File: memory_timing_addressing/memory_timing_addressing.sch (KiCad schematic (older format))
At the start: 1 part, among them P1 DIN_41612_128P

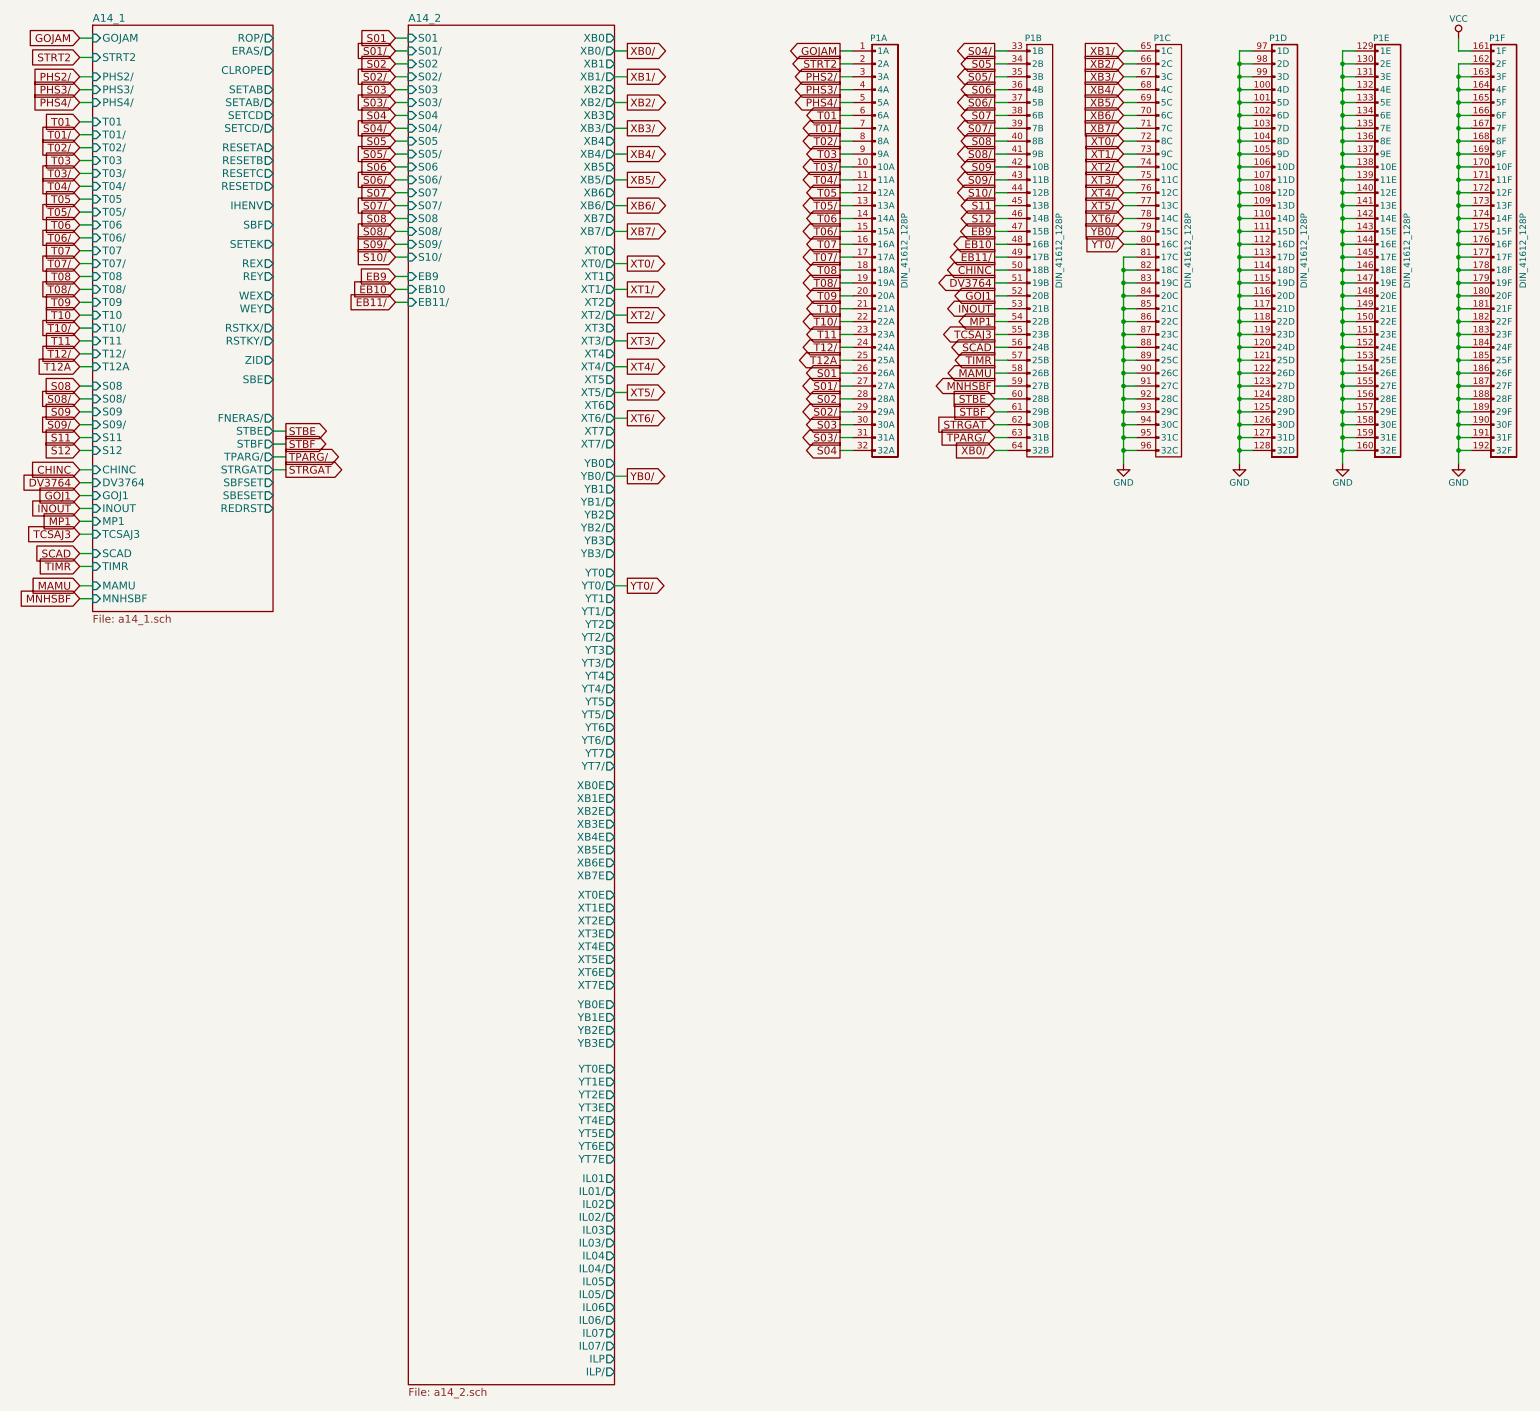
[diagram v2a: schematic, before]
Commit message: New module: custom memory! This uses a flash chip and decodes address based entirely off of rope control signals.
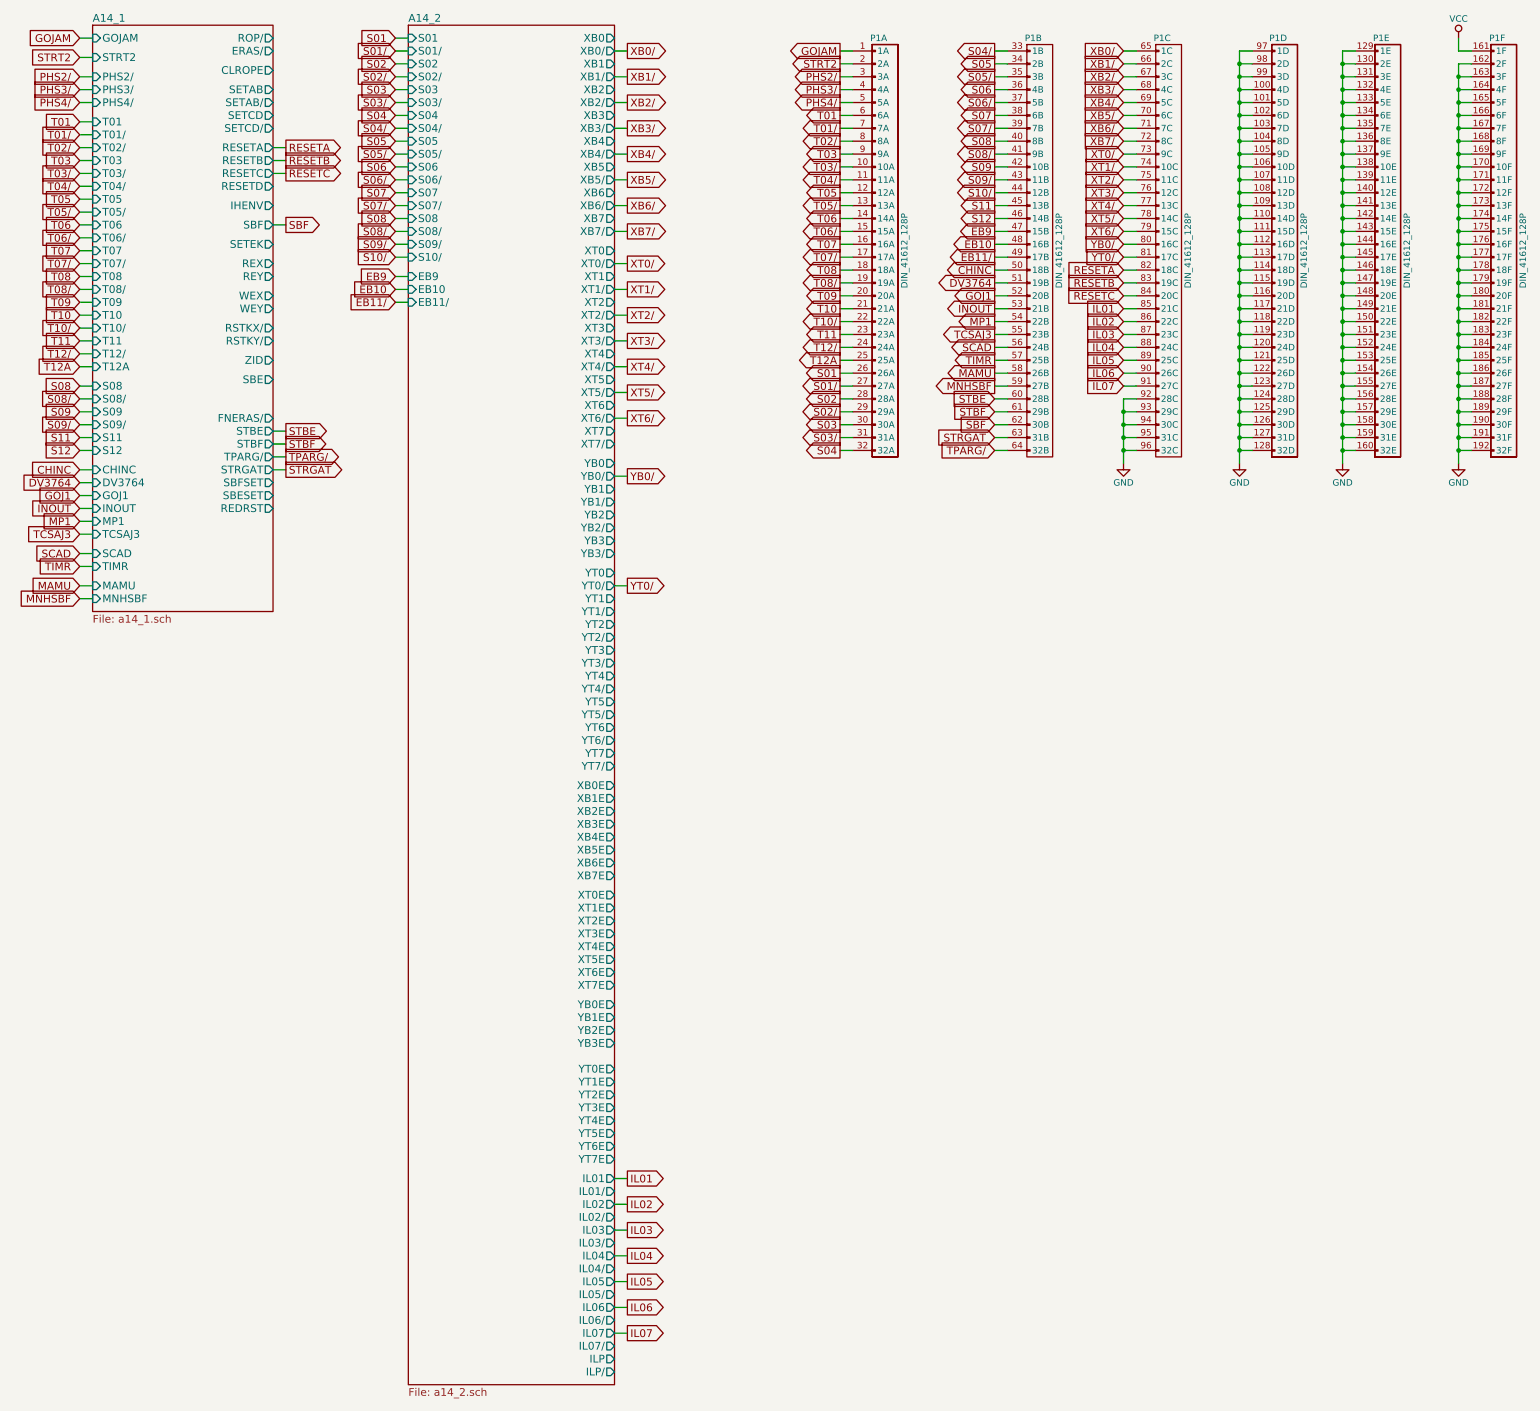
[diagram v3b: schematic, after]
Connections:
- net GND: no longer P1.81 (17C), P1.82 (18C), P1.83 (19C), P1.84 (20C), P1.85 (21C), P1.86 (22C), P1.87 (23C), P1.88 (24C), P1.89 (25C), P1.90 (26C), P1.91 (27C)
- net STRGAT: now also P1.63 (31B); no longer P1.62 (30B)
- net TPARG/: now also P1.64 (32B); no longer P1.63 (31B)
- net XB0/: now also P1.65 (1C); no longer P1.64 (32B)
- net XB1/: now also P1.66 (2C); no longer P1.65 (1C)
- net XB2/: now also P1.67 (3C); no longer P1.66 (2C)
- net XB3/: now also P1.68 (4C); no longer P1.67 (3C)
- net XB4/: now also P1.69 (5C); no longer P1.68 (4C)
- net XB5/: now also P1.70 (6C); no longer P1.69 (5C)
- net XB6/: now also P1.71 (7C); no longer P1.70 (6C)
- net XB7/: now also P1.72 (8C); no longer P1.71 (7C)
- net XT0/: now also P1.73 (9C); no longer P1.72 (8C)
- net XT1/: now also P1.74 (10C); no longer P1.73 (9C)
- net XT2/: now also P1.75 (11C); no longer P1.74 (10C)
- net XT3/: now also P1.76 (12C); no longer P1.75 (11C)
- net XT4/: now also P1.77 (13C); no longer P1.76 (12C)
- net XT5/: now also P1.78 (14C); no longer P1.77 (13C)
- net XT6/: now also P1.79 (15C); no longer P1.78 (14C)
- net YB0/: now also P1.80 (16C); no longer P1.79 (15C)
- net YT0/: now also P1.81 (17C); no longer P1.80 (16C)
- new net IL01: P1.85 (21C)
- new net IL02: P1.86 (22C)
- new net IL03: P1.87 (23C)
- new net IL04: P1.88 (24C)
- new net IL05: P1.89 (25C)
- new net IL06: P1.90 (26C)
- new net IL07: P1.91 (27C)
- new net RESETA: P1.82 (18C)
- new net RESETB: P1.83 (19C)
- new net RESETC: P1.84 (20C)
- new net SBF: P1.62 (30B)
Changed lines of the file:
@@
 $EndComp
 Wire Wire Line
-	9450 3000 9550 3000
-Wire Wire Line
-	9450 3100 9550 3100
-Connection ~ 9450 3100
-Wire Wire Line
-	9450 3200 9550 3200
-Connection ~ 9450 3200
-Wire Wire Line
-	9450 3300 9550 3300
-Connection ~ 9450 3300
-Wire Wire Line
-	9450 3400 9550 3400
-Connection ~ 9450 3400
-Wire Wire Line
-	9450 3500 9550 3500
-Connection ~ 9450 3500
-Wire Wire Line
-	9450 3600 9550 3600
-Connection ~ 9450 3600
-Wire Wire Line
-	9450 3700 9550 3700
-Connection ~ 9450 3700
-Wire Wire Line
-	9450 3800 9550 3800
-Connection ~ 9450 3800
-Wire Wire Line
-	9450 3900 9550 3900
-Connection ~ 9450 3900
-Wire Wire Line
-	9450 4000 9550 4000
-Connection ~ 9450 4000
-Wire Wire Line
 	9450 4100 9550 4100
-Connection ~ 9450 4100
 Wire Wire Line
 	9450 4200 9550 4200
@@
 STBF
 Wire Wire Line
-	8550 4400 8450 4400
-Text GLabel 8450 4400 0    60   Input ~ 0
+	8550 4500 8450 4500
+Text GLabel 8450 4500 0    60   Input ~ 0
 TPARG/
 Wire Wire Line
@@
 XB7/
 Wire Wire Line
-	8550 4500 8450 4500
-Text GLabel 8450 4500 0    60   Input ~ 0
-XB0/
-Wire Wire Line
 	9550 1400 9450 1400
 Text GLabel 9450 1400 0    60   Input ~ 0
-XB1/
+XB0/
 Wire Wire Line
 	9550 1500 9450 1500
 Text GLabel 9450 1500 0    60   Input ~ 0
-XB2/
+XB1/
 Wire Wire Line
 	9550 1600 9450 1600
 Text GLabel 9450 1600 0    60   Input ~ 0
-XB3/
+XB2/
 Wire Wire Line
 	9550 1700 9450 1700
 Text GLabel 9450 1700 0    60   Input ~ 0
-XB4/
+XB3/
 Wire Wire Line
 	9550 1800 9450 1800
 Text GLabel 9450 1800 0    60   Input ~ 0
-XB5/
+XB4/
 Wire Wire Line
 	9550 1900 9450 1900
 Text GLabel 9450 1900 0    60   Input ~ 0
-XB6/
+XB5/
 Wire Wire Line
 	9550 2000 9450 2000
 Text GLabel 9450 2000 0    60   Input ~ 0
+XB6/
+Wire Wire Line
+	9550 2100 9450 2100
+Text GLabel 9450 2100 0    60   Input ~ 0
 XB7/
 Wire Wire Line
@@
 XT6/
 Wire Wire Line
-	9550 2100 9450 2100
-Text GLabel 9450 2100 0    60   Input ~ 0
-XT0/
-Wire Wire Line
 	9550 2200 9450 2200
 Text GLabel 9450 2200 0    60   Input ~ 0
-XT1/
+XT0/
 Wire Wire Line
 	9550 2300 9450 2300
 Text GLabel 9450 2300 0    60   Input ~ 0
-XT2/
+XT1/
 Wire Wire Line
 	9550 2400 9450 2400
 Text GLabel 9450 2400 0    60   Input ~ 0
-XT3/
+XT2/
 Wire Wire Line
 	9550 2500 9450 2500
 Text GLabel 9450 2500 0    60   Input ~ 0
-XT4/
+XT3/
 Wire Wire Line
 	9550 2600 9450 2600
 Text GLabel 9450 2600 0    60   Input ~ 0
-XT5/
+XT4/
 Wire Wire Line
 	9550 2700 9450 2700
 Text GLabel 9450 2700 0    60   Input ~ 0
+XT5/
+Wire Wire Line
+	9550 2800 9450 2800
+Text GLabel 9450 2800 0    60   Input ~ 0
 XT6/
 Wire Wire Line
@@
 YB0/
 Wire Wire Line
-	9550 2800 9450 2800
-Text GLabel 9450 2800 0    60   Input ~ 0
+	9550 2900 9450 2900
+Text GLabel 9450 2900 0    60   Input ~ 0
 YB0/
 Wire Wire Line
@@
 YT0/
 Wire Wire Line
-	9550 2900 9450 2900
-Text GLabel 9450 2900 0    60   Input ~ 0
+	9550 3000 9450 3000
+Text GLabel 9450 3000 0    60   Input ~ 0
 YT0/
 Wire Wire Line
@@
 STRGAT
 Wire Wire Line
-	9450 3000 9450 4600
+	8550 4400 8450 4400
+Text GLabel 8450 4400 0    60   Input ~ 0
+STRGAT
+Wire Wire Line
+	2850 2150 2950 2150
+Text GLabel 2950 2150 2    60   Output ~ 0
+RESETA
+Wire Wire Line
+	2850 2250 2950 2250
+Text GLabel 2950 2250 2    60   Output ~ 0
+RESETB
+Wire Wire Line
+	2850 2350 2950 2350
+Text GLabel 2950 2350 2    60   Output ~ 0
+RESETC
+Wire Wire Line
+	9550 3100 9450 3100
+Text GLabel 9450 3100 0    60   Input ~ 0
+RESETA
+Wire Wire Line
+	9550 3200 9450 3200
+Text GLabel 9450 3200 0    60   Input ~ 0
+RESETB
+Wire Wire Line
+	9550 3300 9450 3300
+Text GLabel 9450 3300 0    60   Input ~ 0
+RESETC
+Wire Wire Line
+	5500 10150 5600 10150
+Text GLabel 5600 10150 2    60   Output ~ 0
+IL01
+Wire Wire Line
+	5500 10350 5600 10350
+Text GLabel 5600 10350 2    60   Output ~ 0
+IL02
+Wire Wire Line
+	5500 10550 5600 10550
+Text GLabel 5600 10550 2    60   Output ~ 0
+IL03
+Wire Wire Line
+	5500 10750 5600 10750
+Text GLabel 5600 10750 2    60   Output ~ 0
+IL04
+Wire Wire Line
+	5500 10950 5600 10950
+Text GLabel 5600 10950 2    60   Output ~ 0
+IL05
+Wire Wire Line
+	5500 11150 5600 11150
+Text GLabel 5600 11150 2    60   Output ~ 0
+IL06
+Wire Wire Line
+	5500 11350 5600 11350
+Text GLabel 5600 11350 2    60   Output ~ 0
+IL07
+Wire Wire Line
+	9550 3400 9450 3400
+Text GLabel 9450 3400 0    60   Input ~ 0
+IL01
+Wire Wire Line
+	9550 3500 9450 3500
+Text GLabel 9450 3500 0    60   Input ~ 0
+IL02
+Wire Wire Line
+	9550 3600 9450 3600
+Text GLabel 9450 3600 0    60   Input ~ 0
+IL03
+Wire Wire Line
+	9550 3700 9450 3700
+Text GLabel 9450 3700 0    60   Input ~ 0
+IL04
+Wire Wire Line
+	9550 3800 9450 3800
+Text GLabel 9450 3800 0    60   Input ~ 0
+IL05
+Wire Wire Line
+	9550 3900 9450 3900
+Text GLabel 9450 3900 0    60   Input ~ 0
+IL06
+Wire Wire Line
+	9550 4000 9450 4000
+Text GLabel 9450 4000 0    60   Input ~ 0
+IL07
+Wire Wire Line
+	2850 2750 2950 2750
+Text GLabel 2950 2750 2    60   Output ~ 0
+SBF
+Wire Wire Line
+	9450 4100 9450 4600
 Wire Wire Line
 	8550 4300 8450 4300
 Text GLabel 8450 4300 0    60   Input ~ 0
-STRGAT
+SBF
 $EndSCHEMATC
